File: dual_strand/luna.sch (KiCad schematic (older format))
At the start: 23 parts, among them J1 Conn_01x06_MountingPin, J2 Conn_01x01, J3 Conn_01x01, Q1 DMN3404L, Q2 DMN3404L, Q3 DMN3404L, Q4 DMN3404L, U1 AP65211AWU, U2 ESP32-WROOM-32, U3 TSOP343xx

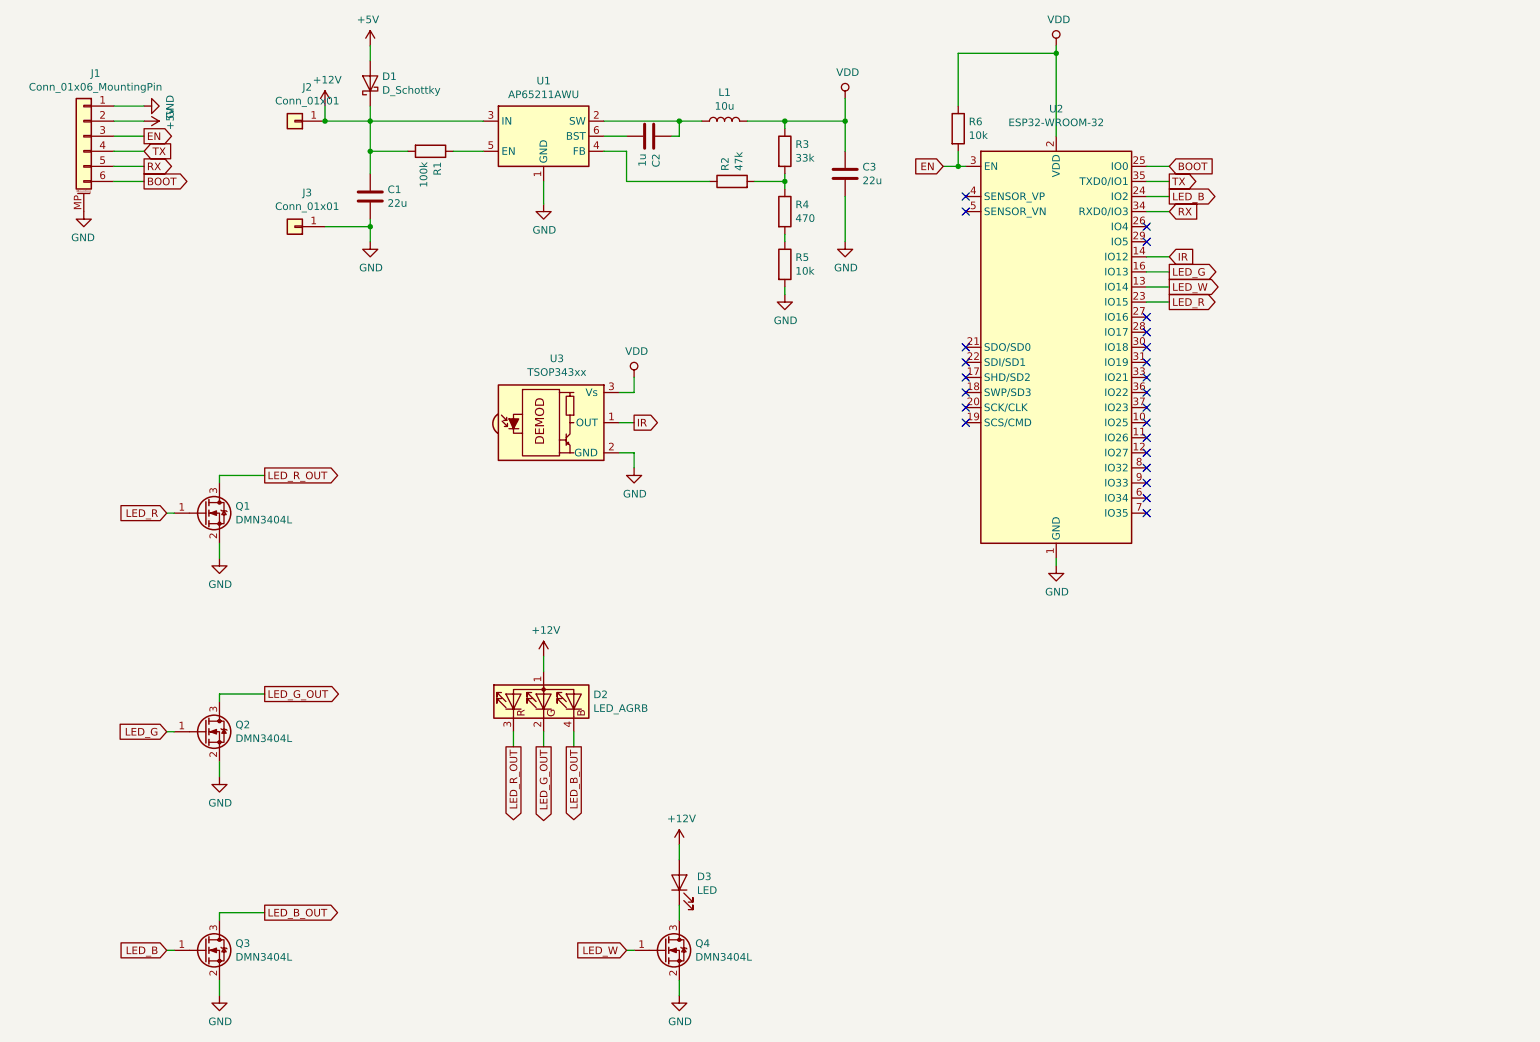
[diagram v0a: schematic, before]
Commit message: Added MOSFET pull-downs. Moved IR receiver to the other side. Shrunk ground plane
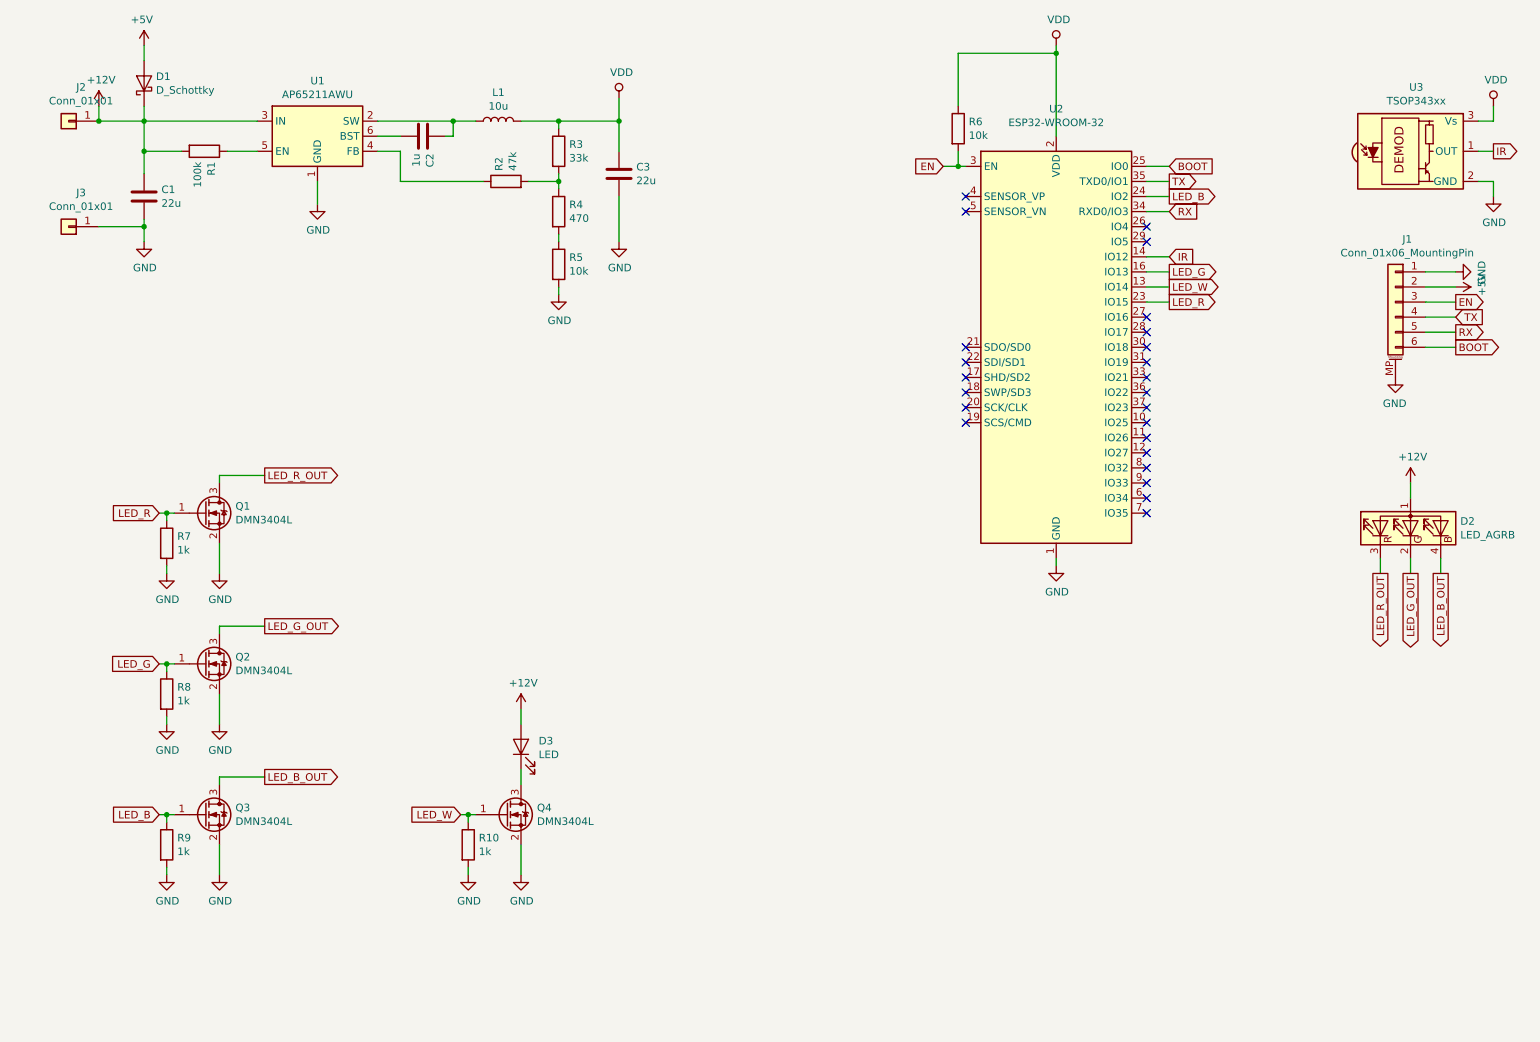
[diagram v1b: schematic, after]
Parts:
- added R10, R7, R8, R9: 1k, Resistor_SMD:R_0805_2012Metric_Pad1.15x1.40mm_HandSolder, symbol Device:R
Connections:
- net GND: now also R10.2, R7.2, R8.2, R9.2
- net LED_B: now also R9.1
- net LED_G: now also R8.1
- net LED_R: now also R7.1
- net LED_W: now also R10.1
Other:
- moved on the sheet: C1, C2, C3, D1, D2, D3, J1, J2, J3, L1, Q2, Q3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
